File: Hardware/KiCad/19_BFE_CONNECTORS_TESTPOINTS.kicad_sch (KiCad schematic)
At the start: 0 parts

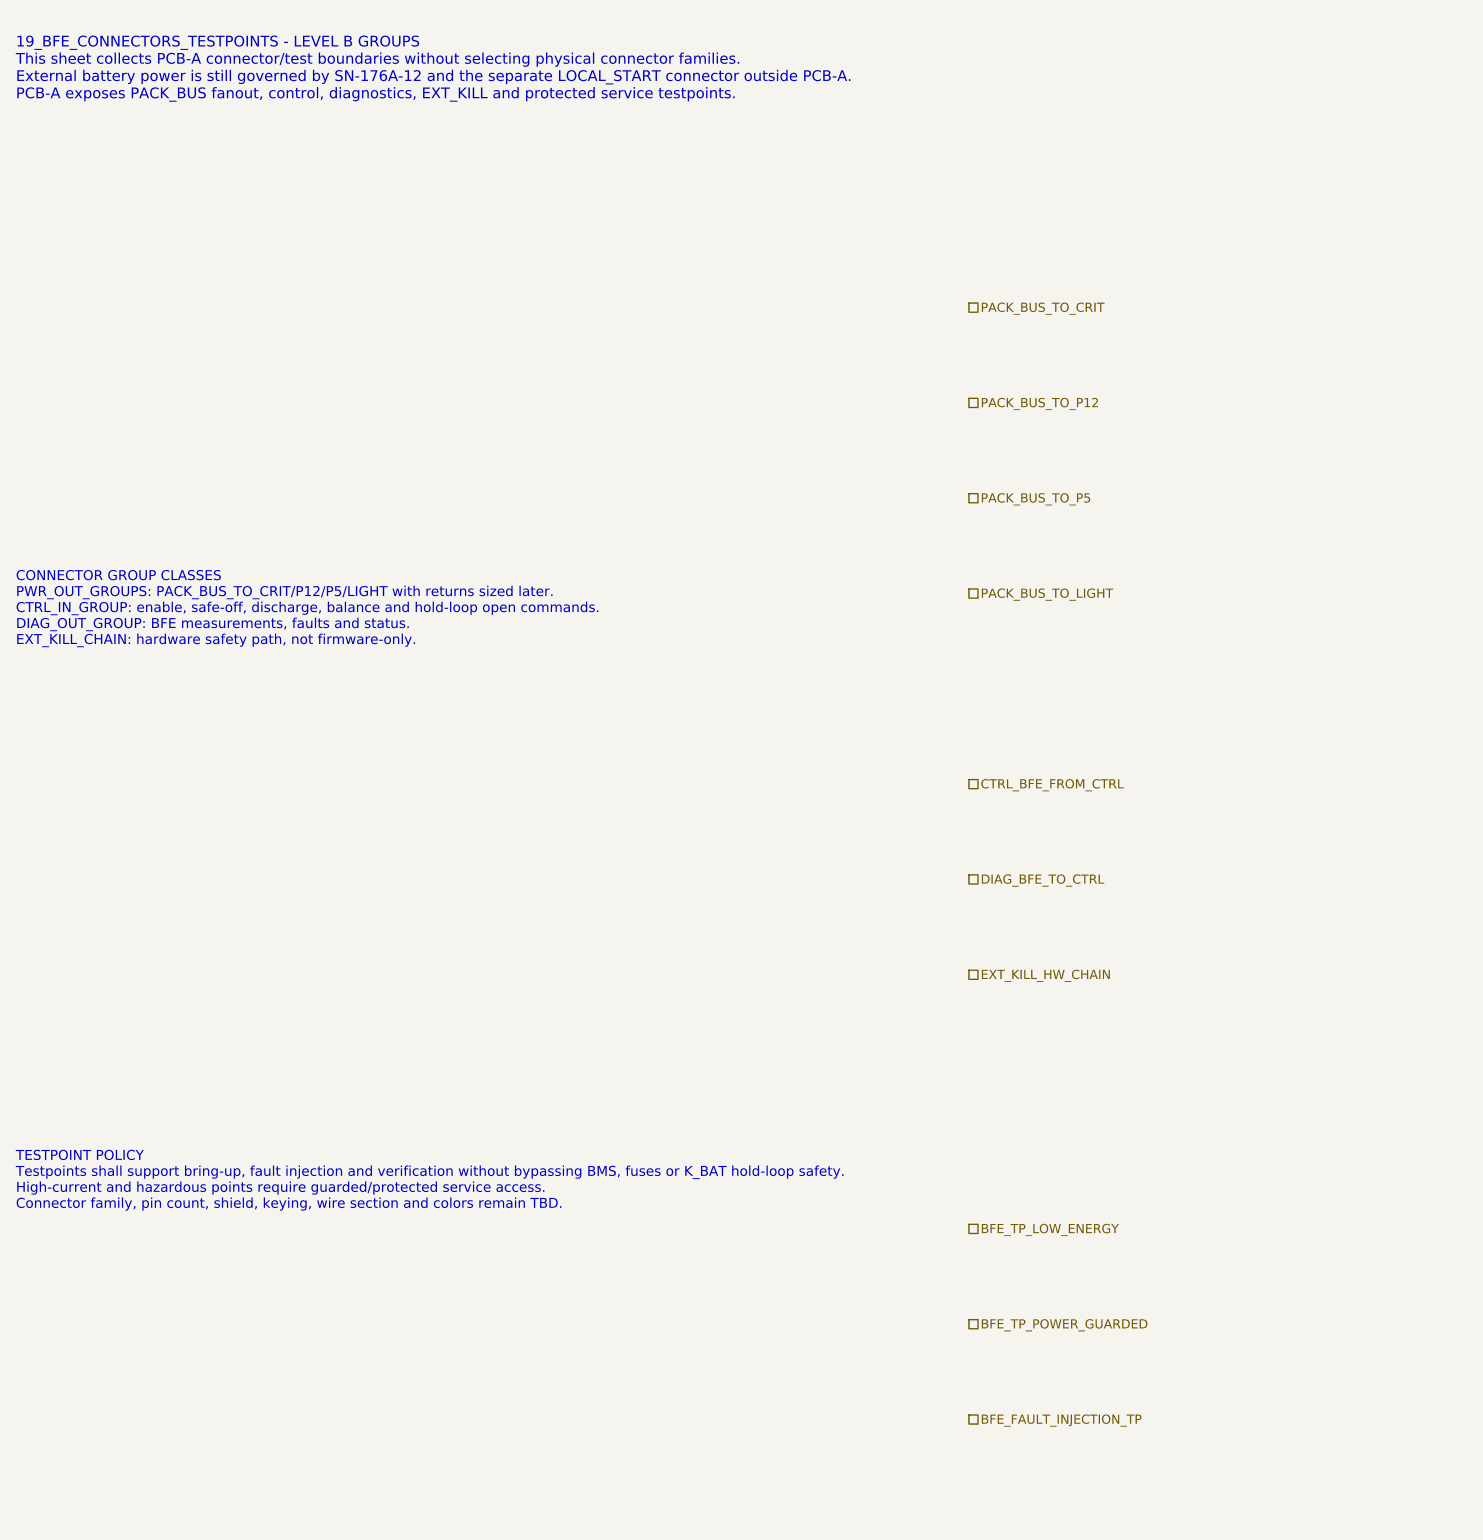
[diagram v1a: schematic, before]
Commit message: hardware: add BFE connector and testpoint skeleton zones
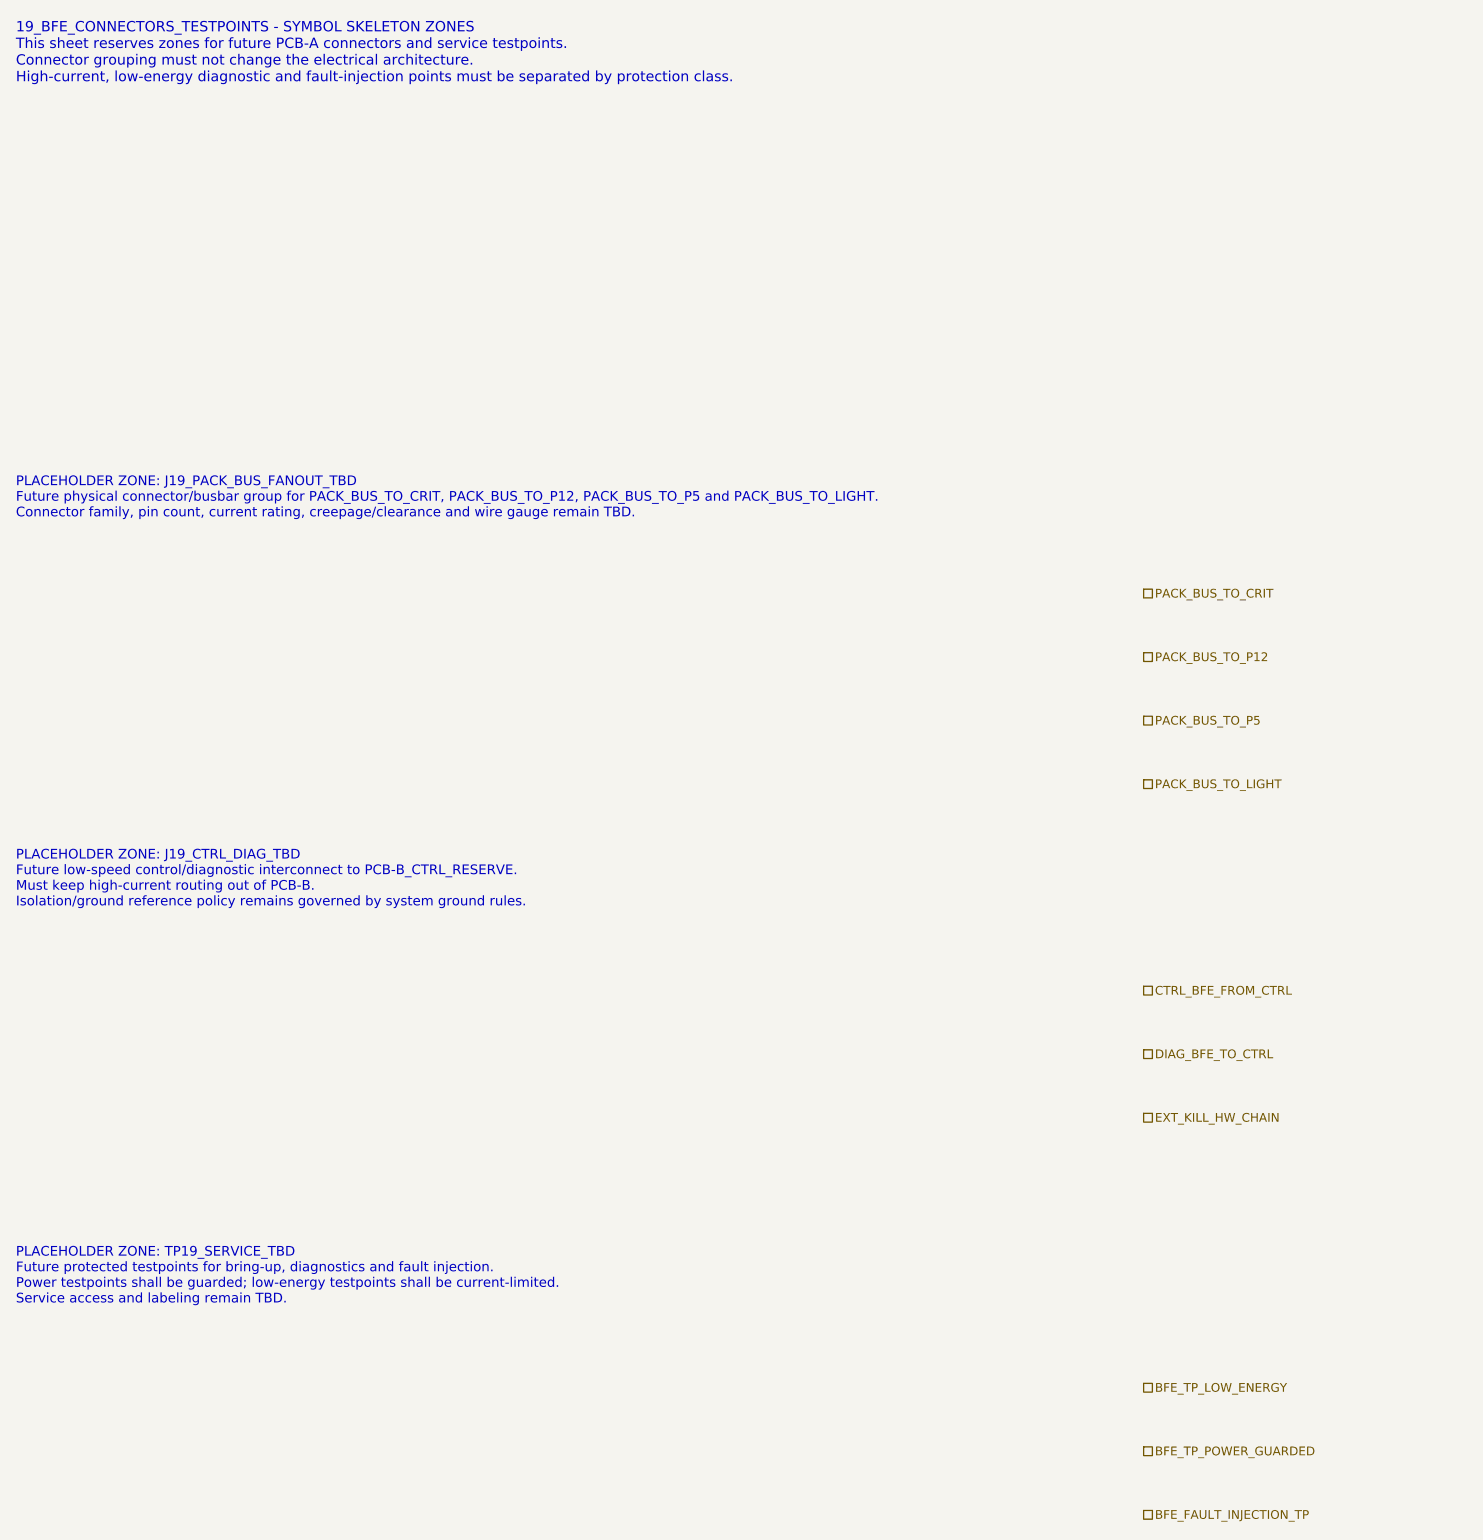
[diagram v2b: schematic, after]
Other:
- note added: "19_BFE_CONNECTORS_TESTPOINTS - SYMBOL SKELETON ZONES This sheet reserves zones for future PCB-A connectors and service testpoints. Connector grouping must not change the electrical architecture. High-current, low-energy diagnostic and fault-injection points must be separated by protection class."
- note added: "PLACEHOLDER ZONE: J19_CTRL_DIAG_TBD Future low-speed control/diagnostic interconnect to PCB-B_CTRL_RESERVE. Must keep high-current routing out of PCB-B. Isolation/ground reference policy remains governed by system ground rules."
- note added: "PLACEHOLDER ZONE: J19_PACK_BUS_FANOUT_TBD Future physical connector/busbar group for PACK_BUS_TO_CRIT, PACK_BUS_TO_P12, PACK_BUS_TO_P5 and PACK_BUS_TO_LIGHT. Connector family, pin count, current rating, creepage/clearance and wire gauge remain TBD."
- note added: "PLACEHOLDER ZONE: TP19_SERVICE_TBD Future protected testpoints for bring-up, diagnostics and fault injection. Power testpoints shall be guarded; low-energy testpoints shall be current-limited. Service access and labeling remain TBD."
- note removed: "19_BFE_CONNECTORS_TESTPOINTS - LEVEL B GROUPS This sheet collects PCB-A connector/test boundaries without selecting physical connector families. External battery power is still governed by SN-176A-12 and the separate LOCAL_START connector outside PCB-A. PCB-A exposes PACK_BUS fanout, control, diagnostics, EXT_KILL and protected service testpoints."
- note removed: "CONNECTOR GROUP CLASSES PWR_OUT_GROUPS: PACK_BUS_TO_CRIT/P12/P5/LIGHT with returns sized later. CTRL_IN_GROUP: enable, safe-off, discharge, balance and hold-loop open commands. DIAG_OUT_GROUP: BFE measurements, faults and status. EXT_KILL_CHAIN: hardware safety path, not firmware-only."
- note removed: "TESTPOINT POLICY Testpoints shall support bring-up, fault injection and verification without bypassing BMS, fuses or K_BAT hold-loop safety. High-current and hazardous points require guarded/protected service access. Connector family, pin count, shield, keying, wire section and colors remain TBD."
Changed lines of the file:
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@@
 		(title "19_BFE_CONNECTORS_TESTPOINTS - BFE connector/test boundary")
 		(date "2026-07-15")
-		(rev "B1")
+		(rev "C1")
 		(company "Gonoboben/plataVM")
-		(comment 1 "Architecture Level B: connector groups and protected testpoint classes")
-		(comment 2 "No connector family, pin count, wire gauge or footprint selected")
+		(comment 1 "Symbol skeleton: BFE connector groups and protected testpoint placeholders")
+		(comment 2 "No connector family, pin count, wire section, footprint or BOM part selected")
 	)
-	(text "19_BFE_CONNECTORS_TESTPOINTS - LEVEL B GROUPS\nThis sheet collects PCB-A connector/test boundaries without selecting physical connector families.\nExternal battery power is still governed by SN-176A-12 and the separate LOCAL_START connector outside PCB-A.\nPCB-A exposes PACK_BUS fanout, control, diagnostics, EXT_KILL and protected service testpoints."
+	(text "19_BFE_CONNECTORS_TESTPOINTS - SYMBOL SKELETON ZONES\nThis sheet reserves zones for future PCB-A connectors and service testpoints.\nConnector grouping must not change the electrical architecture.\nHigh-current, low-energy diagnostic and fault-injection points must be separated by protection class."
 		(exclude_from_sim no)
-		(at 12 18 0)
-		(effects (font (size 1.35 1.35)) (justify left))
+		(at 12 16 0)
+		(effects (font (size 1.3 1.3)) (justify left))
 		(uuid "bfe-lb-00000019-0000-4000-8000-000000000101")
 	)
-	(text "CONNECTOR GROUP CLASSES\nPWR_OUT_GROUPS: PACK_BUS_TO_CRIT/P12/P5/LIGHT with returns sized later.\nCTRL_IN_GROUP: enable, safe-off, discharge, balance and hold-loop open commands.\nDIAG_OUT_GROUP: BFE measurements, faults and status.\nEXT_KILL_CHAIN: hardware safety path, not firmware-only."
+	(text "PLACEHOLDER ZONE: J19_PACK_BUS_FANOUT_TBD\nFuture physical connector/busbar group for PACK_BUS_TO_CRIT, PACK_BUS_TO_P12, PACK_BUS_TO_P5 and PACK_BUS_TO_LIGHT.\nConnector family, pin count, current rating, creepage/clearance and wire gauge remain TBD."
 		(exclude_from_sim no)
-		(at 12 86 0)
-		(effects (font (size 1.25 1.25)) (justify left))
+		(at 12 72 0)
+		(effects (font (size 1.22 1.22)) (justify left))
 		(uuid "bfe-lb-00000019-0000-4000-8000-000000000102")
 	)
-	(text "TESTPOINT POLICY\nTestpoints shall support bring-up, fault injection and verification without bypassing BMS, fuses or K_BAT hold-loop safety.\nHigh-current and hazardous points require guarded/protected service access.\nConnector family, pin count, shield, keying, wire section and colors remain TBD."
+	(text "PLACEHOLDER ZONE: J19_CTRL_DIAG_TBD\nFuture low-speed control/diagnostic interconnect to PCB-B_CTRL_RESERVE.\nMust keep high-current routing out of PCB-B.\nIsolation/ground reference policy remains governed by system ground rules."
 		(exclude_from_sim no)
-		(at 12 158 0)
-		(effects (font (size 1.25 1.25)) (justify left))
+		(at 12 120 0)
+		(effects (font (size 1.22 1.22)) (justify left))
 		(uuid "bfe-lb-00000019-0000-4000-8000-000000000103")
 	)
-	(hierarchical_label "PACK_BUS_TO_CRIT" (shape passive) (exclude_from_sim no) (at 132 48 0) (effects (font (size 1.15 1.15)) (justify left)) (uuid "bfe-lb-00000019-0000-4000-8000-000000000201"))
-	(hierarchical_label "PACK_BUS_TO_P12" (shape passive) (exclude_from_sim no) (at 132 60 0) (effects (font (size 1.15 1.15)) (justify left)) (uuid "bfe-lb-00000019-0000-4000-8000-000000000202"))
-	(hierarchical_label "PACK_BUS_TO_P5" (shape passive) (exclude_from_sim no) (at 132 72 0) (effects (font (size 1.15 1.15)) (justify left)) (uuid "bfe-lb-00000019-0000-4000-8000-000000000203"))
-	(hierarchical_label "PACK_BUS_TO_LIGHT" (shape passive) (exclude_from_sim no) (at 132 84 0) (effects (font (size 1.15 1.15)) (justify left)) (uuid "bfe-lb-00000019-0000-4000-8000-000000000204"))
-	(hierarchical_label "CTRL_BFE_FROM_CTRL" (shape passive) (exclude_from_sim no) (at 132 108 0) (effects (font (size 1.15 1.15)) (justify left)) (uuid "bfe-lb-00000019-0000-4000-8000-000000000205"))
-	(hierarchical_label "DIAG_BFE_TO_CTRL" (shape passive) (exclude_from_sim no) (at 132 120 0) (effects (font (size 1.15 1.15)) (justify left)) (uuid "bfe-lb-00000019-0000-4000-8000-000000000206"))
-	(hierarchical_label "EXT_KILL_HW_CHAIN" (shape passive) (exclude_from_sim no) (at 132 132 0) (effects (font (size 1.15 1.15)) (justify left)) (uuid "bfe-lb-00000019-0000-4000-8000-000000000207"))
-	(hierarchical_label "BFE_TP_LOW_ENERGY" (shape passive) (exclude_from_sim no) (at 132 164 0) (effects (font (size 1.15 1.15)) (justify left)) (uuid "bfe-lb-00000019-0000-4000-8000-000000000208"))
-	(hierarchical_label "BFE_TP_POWER_GUARDED" (shape passive) (exclude_from_sim no) (at 132 176 0) (effects (font (size 1.15 1.15)) (justify left)) (uuid "bfe-lb-00000019-0000-4000-8000-000000000209"))
-	(hierarchical_label "BFE_FAULT_INJECTION_TP" (shape passive) (exclude_from_sim no) (at 132 188 0) (effects (font (size 1.15 1.15)) (justify left)) (uuid "bfe-lb-00000019-0000-4000-8000-000000000210"))
+	(text "PLACEHOLDER ZONE: TP19_SERVICE_TBD\nFuture protected testpoints for bring-up, diagnostics and fault injection.\nPower testpoints shall be guarded; low-energy testpoints shall be current-limited.\nService access and labeling remain TBD."
+		(exclude_from_sim no)
+		(at 12 170 0)
+		(effects (font (size 1.22 1.22)) (justify left))
+		(uuid "bfe-lb-00000019-0000-4000-8000-000000000104")
+	)
+	(hierarchical_label "PACK_BUS_TO_CRIT" (shape passive) (exclude_from_sim no) (at 154 84 0) (effects (font (size 1.1 1.1)) (justify left)) (uuid "bfe-lb-00000019-0000-4000-8000-000000000201"))
+	(hierarchical_label "PACK_BUS_TO_P12" (shape passive) (exclude_from_sim no) (at 154 92 0) (effects (font (size 1.1 1.1)) (justify left)) (uuid "bfe-lb-00000019-0000-4000-8000-000000000202"))
+	(hierarchical_label "PACK_BUS_TO_P5" (shape passive) (exclude_from_sim no) (at 154 100 0) (effects (font (size 1.1 1.1)) (justify left)) (uuid "bfe-lb-00000019-0000-4000-8000-000000000203"))
+	(hierarchical_label "PACK_BUS_TO_LIGHT" (shape passive) (exclude_from_sim no) (at 154 108 0) (effects (font (size 1.1 1.1)) (justify left)) (uuid "bfe-lb-00000019-0000-4000-8000-000000000204"))
+	(hierarchical_label "CTRL_BFE_FROM_CTRL" (shape passive) (exclude_from_sim no) (at 154 134 0) (effects (font (size 1.1 1.1)) (justify left)) (uuid "bfe-lb-00000019-0000-4000-8000-000000000205"))
+	(hierarchical_label "DIAG_BFE_TO_CTRL" (shape passive) (exclude_from_sim no) (at 154 142 0) (effects (font (size 1.1 1.1)) (justify left)) (uuid "bfe-lb-00000019-0000-4000-8000-000000000206"))
+	(hierarchical_label "EXT_KILL_HW_CHAIN" (shape passive) (exclude_from_sim no) (at 154 150 0) (effects (font (size 1.1 1.1)) (justify left)) (uuid "bfe-lb-00000019-0000-4000-8000-000000000207"))
+	(hierarchical_label "BFE_TP_LOW_ENERGY" (shape passive) (exclude_from_sim no) (at 154 184 0) (effects (font (size 1.1 1.1)) (justify left)) (uuid "bfe-lb-00000019-0000-4000-8000-000000000208"))
+	(hierarchical_label "BFE_TP_POWER_GUARDED" (shape passive) (exclude_from_sim no) (at 154 192 0) (effects (font (size 1.1 1.1)) (justify left)) (uuid "bfe-lb-00000019-0000-4000-8000-000000000209"))
+	(hierarchical_label "BFE_FAULT_INJECTION_TP" (shape passive) (exclude_from_sim no) (at 154 200 0) (effects (font (size 1.1 1.1)) (justify left)) (uuid "bfe-lb-00000019-0000-4000-8000-000000000210"))
 )
